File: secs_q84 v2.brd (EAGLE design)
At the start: 102.5 x 69.8 mm, 134 parts, among them IC1 MAX203ECWP, IC2 REF3440TIDBVR, IC3 ADP151AUJZ-3.3-R7, IC4 ADM3095EBRZ, IC5 MCZ33996EK, IC6 74HC125D, IC7 TIC12400DCPR, IC8 PIC18F57Q84-I_PT

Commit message: cal analog inputs
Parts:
- renumbered LED1 to LED1_RED
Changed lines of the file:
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@@
 <layer number="14" name="Route14" color="22" fill="1" visible="no" active="no"/>
 <layer number="15" name="Route15" color="23" fill="1" visible="no" active="yes"/>
-<layer number="16" name="Bottom" color="1" fill="1" visible="yes" active="yes"/>
+<layer number="16" name="Bottom" color="1" fill="1" visible="no" active="yes"/>
 <layer number="17" name="Pads" color="2" fill="1" visible="yes" active="yes"/>
 <layer number="18" name="Vias" color="2" fill="1" visible="yes" active="yes"/>
 <layer number="19" name="Unrouted" color="6" fill="1" visible="yes" active="yes"/>
 <layer number="20" name="Dimension" color="24" fill="1" visible="yes" active="yes"/>
-<layer number="21" name="tPlace" color="7" fill="1" visible="no" active="yes"/>
-<layer number="22" name="bPlace" color="7" fill="1" visible="yes" active="yes"/>
-<layer number="23" name="tOrigins" color="15" fill="1" visible="no" active="yes"/>
-<layer number="24" name="bOrigins" color="15" fill="1" visible="yes" active="yes"/>
-<layer number="25" name="tNames" color="7" fill="1" visible="no" active="yes"/>
-<layer number="26" name="bNames" color="7" fill="1" visible="yes" active="yes"/>
+<layer number="21" name="tPlace" color="7" fill="1" visible="yes" active="yes"/>
+<layer number="22" name="bPlace" color="7" fill="1" visible="no" active="yes"/>
+<layer number="23" name="tOrigins" color="15" fill="1" visible="yes" active="yes"/>
+<layer number="24" name="bOrigins" color="15" fill="1" visible="no" active="yes"/>
+<layer number="25" name="tNames" color="7" fill="1" visible="yes" active="yes"/>
+<layer number="26" name="bNames" color="7" fill="1" visible="no" active="yes"/>
 <layer number="27" name="tValues" color="7" fill="1" visible="no" active="yes"/>
 <layer number="28" name="bValues" color="7" fill="1" visible="no" active="yes"/>
@@
 <layer number="37" name="tTest" color="7" fill="1" visible="no" active="yes"/>
 <layer number="38" name="bTest" color="7" fill="1" visible="no" active="yes"/>
-<layer number="39" name="tKeepout" color="4" fill="11" visible="no" active="yes"/>
-<layer number="40" name="bKeepout" color="1" fill="11" visible="yes" active="yes"/>
-<layer number="41" name="tRestrict" color="4" fill="10" visible="no" active="yes"/>
-<layer number="42" name="bRestrict" color="1" fill="10" visible="yes" active="yes"/>
+<layer number="39" name="tKeepout" color="4" fill="11" visible="yes" active="yes"/>
+<layer number="40" name="bKeepout" color="1" fill="11" visible="no" active="yes"/>
+<layer number="41" name="tRestrict" color="4" fill="10" visible="yes" active="yes"/>
+<layer number="42" name="bRestrict" color="1" fill="10" visible="no" active="yes"/>
 <layer number="43" name="vRestrict" color="2" fill="10" visible="no" active="yes"/>
 <layer number="44" name="Drills" color="7" fill="1" visible="no" active="yes"/>
@@
 <layer number="48" name="Document" color="7" fill="1" visible="no" active="yes"/>
 <layer number="49" name="Reference" color="7" fill="1" visible="no" active="yes"/>
-<layer number="51" name="tDocu" color="7" fill="1" visible="no" active="yes"/>
-<layer number="52" name="bDocu" color="7" fill="1" visible="yes" active="yes"/>
+<layer number="51" name="tDocu" color="7" fill="1" visible="yes" active="yes"/>
+<layer number="52" name="bDocu" color="7" fill="1" visible="no" active="yes"/>
 <layer number="88" name="SimResults" color="9" fill="1" visible="no" active="no"/>
 <layer number="89" name="SimProbes" color="9" fill="1" visible="no" active="no"/>
@@
 <attribute name="VALUE" x="22.479" y="63.5" size="1.27" layer="27" ratio="10" rot="R270"/>
 </element>
-<element name="LED1" library="led" library_urn="urn:adsk.eagle:library:259" package="CHIPLED_0805" package3d_urn="urn:adsk.eagle:package:15821/2" value="L1" x="30.48" y="39.37" smashed="yes" rot="R90">
-<attribute name="NAME" x="36.83" y="40.64" size="1.27" layer="25" rot="R180"/>
+<element name="LED1_RED" library="led" library_urn="urn:adsk.eagle:library:259" package="CHIPLED_0805" package3d_urn="urn:adsk.eagle:package:15821/2" value="L1" x="30.48" y="39.37" smashed="yes" rot="R90">
+<attribute name="NAME" x="36.83" y="41.91" size="1.27" layer="25" rot="R180"/>
 <attribute name="POPULARITY" value="52" x="100.33" y="81.28" size="1.778" layer="27" rot="R90" display="off"/>
 <attribute name="VALUE" x="31.75" y="41.91" size="1.27" layer="27" rot="R180"/>
@@
 <contactref element="C12" pad="2"/>
 <contactref element="MISC_IO" pad="9"/>
-<contactref element="LED1" pad="C"/>
+<contactref element="LED1_RED" pad="C"/>
 <contactref element="LED2" pad="C"/>
 <contactref element="LED3" pad="C"/>
@@
 </signal>
 <signal name="N$4">
-<contactref element="LED1" pad="A"/>
+<contactref element="LED1_RED" pad="A"/>
 <contactref element="R7" pad="1"/>
 <wire x1="31.4706" y1="38.3286" x2="31.4706" y2="39.3192" width="0.1524" layer="1"/>

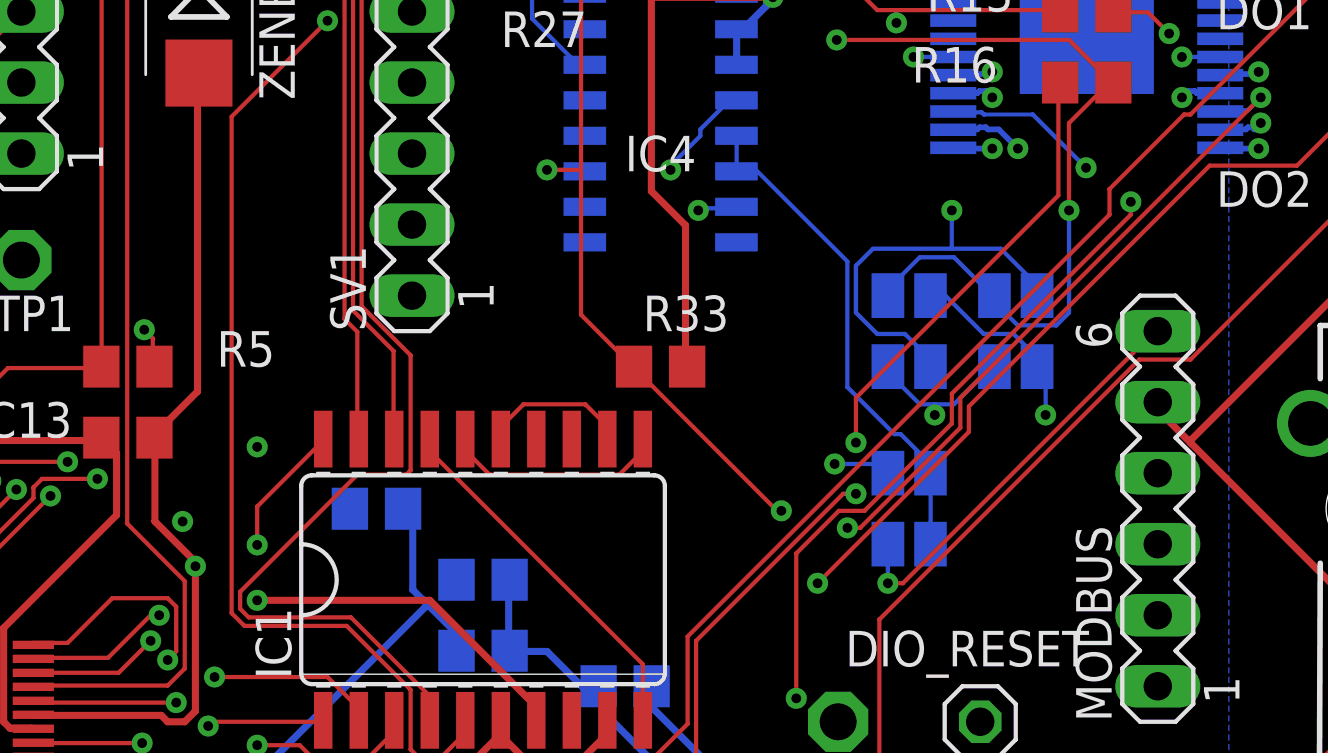
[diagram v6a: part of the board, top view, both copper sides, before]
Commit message: add new code for serial interfaces
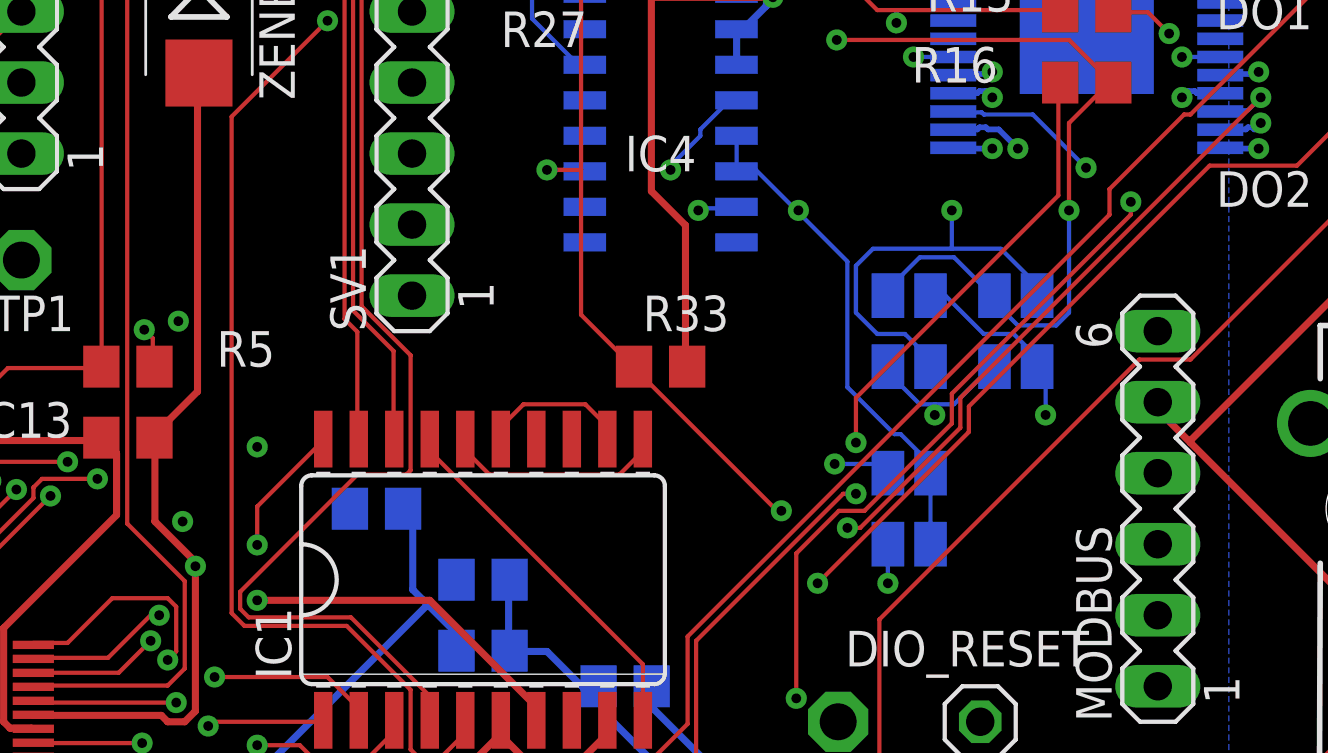
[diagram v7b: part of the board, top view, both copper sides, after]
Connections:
- net DE3: no longer MODBUS.6
- net DERE: now also MODBUS.6
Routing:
- net DE3: track 68.8 -> 52.6 mm, vias 2 -> 3
- net DERE: track 18.1 -> 32.8 mm, vias 0 -> 1
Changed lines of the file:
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@@
 <layers>
 <layer number="1" name="Top" color="4" fill="1" visible="yes" active="yes"/>
-<layer number="2" name="Route2" color="16" fill="1" visible="no" active="yes"/>
+<layer number="2" name="Route2" color="16" fill="1" visible="yes" active="yes"/>
 <layer number="3" name="Route3" color="17" fill="1" visible="no" active="no"/>
 <layer number="4" name="Route4" color="18" fill="1" visible="no" active="no"/>
@@
 <layer number="13" name="Route13" color="21" fill="1" visible="no" active="no"/>
 <layer number="14" name="Route14" color="22" fill="1" visible="no" active="no"/>
-<layer number="15" name="Route15" color="23" fill="1" visible="no" active="yes"/>
-<layer number="16" name="Bottom" color="1" fill="1" visible="no" active="yes"/>
+<layer number="15" name="Route15" color="23" fill="1" visible="yes" active="yes"/>
+<layer number="16" name="Bottom" color="1" fill="1" visible="yes" active="yes"/>
 <layer number="17" name="Pads" color="2" fill="1" visible="yes" active="yes"/>
 <layer number="18" name="Vias" color="2" fill="1" visible="yes" active="yes"/>
@@
 <wire x1="84.582" y1="46.99" x2="84.582" y2="44.45" width="0.1524" layer="16"/>
 <wire x1="78.3336" y1="57.8358" x2="77.724" y2="57.8358" width="0.1524" layer="16"/>
-<wire x1="81.6102" y1="54.5592" x2="78.3336" y2="57.8358" width="0.1524" layer="16"/>
+<wire x1="81.6102" y1="54.5592" x2="79.8195" y2="56.3499" width="0.1524" layer="16"/>
+<wire x1="79.8195" y1="56.3499" x2="78.3336" y2="57.8358" width="0.1524" layer="16"/>
 <wire x1="81.6102" y1="50.0634" x2="81.6102" y2="54.5592" width="0.1524" layer="16"/>
 <wire x1="83.2866" y1="48.387" x2="81.6102" y2="50.0634" width="0.1524" layer="16"/>
@@
 <wire x1="84.582" y1="46.99" x2="84.582" y2="47.3202" width="0.1524" layer="16"/>
 <wire x1="77.724" y1="57.8358" x2="77.642" y2="57.785" width="0.1524" layer="16"/>
+<contactref element="MODBUS" pad="6"/>
+<wire x1="84.1248" y1="52.1208" x2="92.6592" y2="52.1208" width="0.1524" layer="2"/>
+<wire x1="79.8576" y1="56.388" x2="84.1248" y2="52.1208" width="0.1524" layer="2"/>
+<wire x1="92.6592" y1="52.1208" x2="92.71" y2="52.07" width="0.1524" layer="2"/>
+<wire x1="79.8576" y1="56.388" x2="79.8195" y2="56.3499" width="0.1524" layer="16"/>
+<via x="79.8576" y="56.388" extent="1-16" drill="0.35"/>
 </signal>
 <signal name="MOD_TX">
@@
 <signal name="DE3">
 <contactref element="IC8" pad="39"/>
-<contactref element="MODBUS" pad="6"/>
 <contactref element="DE3" pad="2"/>
 <wire x1="50.0634" y1="44.577" x2="50.0634" y2="42.3672" width="0.1524" layer="1"/>
 <wire x1="51.8922" y1="46.4058" x2="50.0634" y2="44.577" width="0.1524" layer="1"/>
-<wire x1="51.8922" y1="47.4726" x2="51.8922" y2="46.4058" width="0.1524" layer="2"/>
-<wire x1="55.9308" y1="51.5112" x2="51.8922" y2="47.4726" width="0.1524" layer="2"/>
-<wire x1="66.294" y1="51.5112" x2="55.9308" y2="51.5112" width="0.1524" layer="2"/>
-<wire x1="73.2282" y1="58.4454" x2="66.294" y2="51.5112" width="0.1524" layer="2"/>
-<wire x1="84.7344" y1="58.4454" x2="73.2282" y2="58.4454" width="0.1524" layer="2"/>
-<wire x1="91.059" y1="52.1208" x2="84.7344" y2="58.4454" width="0.1524" layer="2"/>
-<wire x1="92.6592" y1="52.1208" x2="91.059" y2="52.1208" width="0.1524" layer="2"/>
 <wire x1="50.0634" y1="42.3672" x2="50.01" y2="42.338" width="0.1524" layer="1"/>
-<wire x1="92.6592" y1="52.1208" x2="92.71" y2="52.07" width="0.1524" layer="2"/>
 <wire x1="83.058" y1="43.053" x2="83.058" y2="44.45" width="0.1524" layer="16"/>
-<wire x1="83.5914" y1="43.053" x2="83.058" y2="43.053" width="0.1524" layer="1"/>
-<wire x1="92.6592" y1="52.1208" x2="83.5914" y2="43.053" width="0.1524" layer="1"/>
-<wire x1="92.6592" y1="52.1208" x2="92.71" y2="52.07" width="0.1524" layer="1"/>
 <via x="51.8922" y="46.4058" extent="1-16" drill="0.35"/>
 <via x="83.058" y="43.053" extent="1-16" drill="0.35"/>
+<wire x1="83.058" y1="48.9204" x2="83.058" y2="43.053" width="0.1524" layer="15"/>
+<wire x1="76.8858" y1="55.0926" x2="83.058" y2="48.9204" width="0.1524" layer="15"/>
+<wire x1="76.8858" y1="56.6928" x2="76.8858" y2="55.0926" width="0.1524" layer="15"/>
+<wire x1="76.581" y1="56.9976" x2="76.8858" y2="56.6928" width="0.1524" layer="15"/>
+<wire x1="62.2554" y1="56.9976" x2="76.581" y2="56.9976" width="0.1524" layer="15"/>
+<wire x1="57.6834" y1="52.4256" x2="62.2554" y2="56.9976" width="0.1524" layer="15"/>
+<wire x1="56.769" y1="51.5112" x2="57.6834" y2="52.4256" width="0.1524" layer="2"/>
+<wire x1="55.9308" y1="51.5112" x2="56.769" y2="51.5112" width="0.1524" layer="2"/>
+<wire x1="51.8922" y1="47.4726" x2="55.9308" y2="51.5112" width="0.1524" layer="2"/>
+<wire x1="51.8922" y1="46.4058" x2="51.8922" y2="47.4726" width="0.1524" layer="2"/>
+<via x="57.6834" y="52.4256" extent="1-16" drill="0.35"/>
 </signal>
 <signal name="RF4">

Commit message: up
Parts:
- R28, R29: value 400 ohm -> 390 ohm
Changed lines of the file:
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@@
 <attribute name="VALUE" x="58.42" y="21.59" size="1.27" layer="28" rot="MR0"/>
 </element>
-<element name="R28" library="rcl" library_urn="urn:adsk.eagle:library:334" package="R0805" package3d_urn="urn:adsk.eagle:package:23553/2" value="400 ohm" x="69.85" y="34.29" smashed="yes" rot="MR0">
+<element name="R28" library="rcl" library_urn="urn:adsk.eagle:library:334" package="R0805" package3d_urn="urn:adsk.eagle:package:23553/2" value="390 ohm" x="69.85" y="34.29" smashed="yes" rot="MR0">
 <attribute name="NAME" x="70.485" y="35.56" size="1.27" layer="26" rot="MR0"/>
 <attribute name="POPULARITY" value="85" x="69.85" y="34.29" size="1.778" layer="28" rot="MR0" display="off"/>
@@
 <attribute name="VALUE" x="70.485" y="31.75" size="1.27" layer="28" rot="MR0"/>
 </element>
-<element name="R29" library="rcl" library_urn="urn:adsk.eagle:library:334" package="R0805" package3d_urn="urn:adsk.eagle:package:23553/2" value="400 ohm" x="69.85" y="31.75" smashed="yes" rot="MR0">
+<element name="R29" library="rcl" library_urn="urn:adsk.eagle:library:334" package="R0805" package3d_urn="urn:adsk.eagle:package:23553/2" value="390 ohm" x="69.85" y="31.75" smashed="yes" rot="MR0">
 <attribute name="NAME" x="71.755" y="27.94" size="1.27" layer="26" rot="MR0"/>
 <attribute name="POPULARITY" value="85" x="69.85" y="31.75" size="1.778" layer="28" rot="MR0" display="off"/>
